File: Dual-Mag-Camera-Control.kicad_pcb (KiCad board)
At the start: 4 copper layers, 152.4 x 96.5 mm, 173 parts, among them J1 ~TRIG_IO, J10 RS-232_2_3, J11 PWR_IN_1, J12 PWR_IN_2, J13 STRB_PWR, J14 CAM_COMPUTE_PWR, J15 5V_5A_PWR, J16 5V_2.5A_PWR, J2 TRIG_IO, J3 ADC_DAC, J4 GPIO, J5 CVS-04TB, J6 CVS-04TB, J7 UART_0_1, J8 UART_2_3, J9 RS-232_0_1, Q1 Si7463DP, Q2 Si7463DP, Q3 Si7463DP, Q4 Si7463DP, Q5 SISS12DN, Q6 Si7463DP, Q7 SISS12DN, Q8 Si7463DP, Q9 Si7463DP, U1 D24V10F5, U10 BME280, U11 S18V20F12, U12 S18V20F12, U13 LTC4412HVIS6, U14 LTC4412HVIS6, U15 LTC4412HVIS6, U16 LTC4412HVIS6, U17 LTC4412HVIS6, U18 DS3231M, U2 INA260, U3 D24V50F5, U4 LowPowerLab-SD-Card, U5 D24V22F5, U6 INA260, U8 MoteinoM0

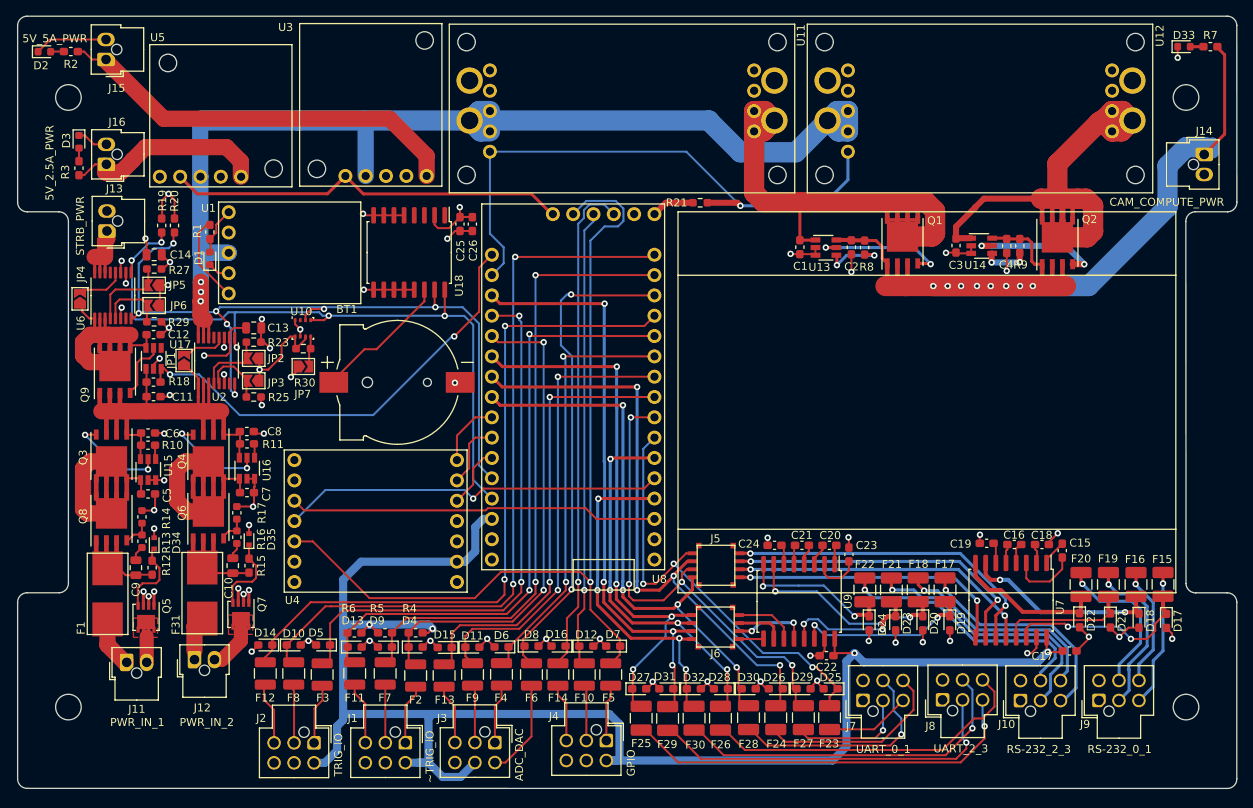
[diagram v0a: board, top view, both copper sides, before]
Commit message: Moved Connectors, NEW PTC Footprint
updated ptc footprints to 0603. Relocated GPIO connectors J1-J4
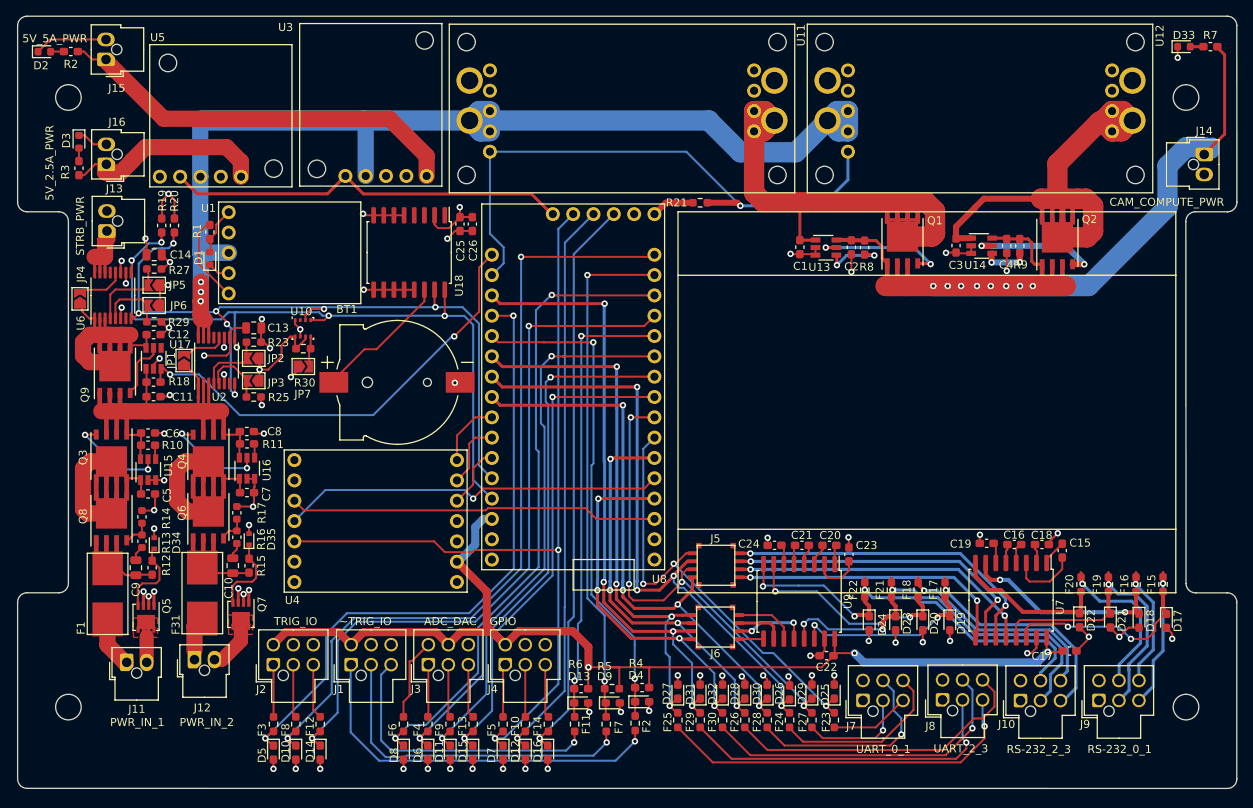
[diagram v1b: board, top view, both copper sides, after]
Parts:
- F10, F11, F12, F13, F14, F2, F3, F4, F5, F6, F7, F8, F9: footprint Resistor_SMD:R_1210_3225Metric -> Resistor_SMD:R_0603_1608Metric_Pad0.98x0.95mm_HandSolder
- F15, F16, F17, F18, F19, F20, F21, F22, F23, F24, F25, F26, F27, F28, F29, F30: footprint Resistor_SMD:R_1210_3225Metric_Pad1.42x2.65mm_HandSolder -> Resistor_SMD:R_0603_1608Metric_Pad0.98x0.95mm_HandSolder
- R5: footprint Resistor_SMD:R_0603_1608Metric_Pad1.05x0.95mm_HandSolder -> Resistor_SMD:R_0603_1608Metric_Pad0.98x0.95mm_HandSolder
- moved D9 29.3 mm to (120.1, 136.0), turned to 0 degrees
- moved R5 29.2 mm to (120.0, 134.3), turned to 0 degrees
- moved R6 29.2 mm to (116.1, 134.3)
- moved D13 29.2 mm to (116.1, 136.0)
- moved D4 29.1 mm to (123.7, 135.9)
- moved R4 29.1 mm to (123.7, 134.1)
- moved F7 28.4 mm to (119.2, 138.7)
- moved F11 28.2 mm to (115.3, 138.7)
- moved F2 28.1 mm to (122.9, 138.6)
- moved D8 20.8 mm to (93.9, 142.2), turned to -90 degrees
- moved D7 19.1 mm to (106.3, 142.2), turned to -90 degrees
- moved F6 17.2 mm to (93.9, 138.7), turned to 90 degrees
- moved D6 16.1 mm to (97.0, 142.2), turned to -90 degrees
- moved J4 15.8 mm to (106.6, 131.2), turned to 90 degrees
- moved D12 15.3 mm to (109.1, 142.2), turned to -90 degrees
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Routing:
- net /3.3V_LDO: track 390.2 -> 333.0 mm, vias 11 -> 10
- net /5V_reg: track 154.1 -> 102.1 mm
- net /TRIG0_1_IO: track 8.44 -> 47.8 mm, vias 0 -> 1
- net /TRIG1_1_IO: track 7.26 -> 42.1 mm, vias 0 -> 1
- net /TRIG4_1_IO: track 7.81 -> 36.5 mm, vias 0 -> 1
- net /COMMS/TX2: track 22.1 -> 50.1 mm, vias 2 -> 3
- net /COMMS/TX2_OUT: track 28.0 -> 0.00 mm, vias 1 -> 0
- net /TRIG4_1: track 78.3 -> 57.3 mm
- net /DAC_OUT: track 61.0 -> 80.7 mm
- net /A3: track 53.6 -> 70.6 mm
- net /GPIO_2: track 57.2 -> 72.2 mm
- net /TRIG1_1: track 78.9 -> 64.6 mm
- net /TRIG0_0: track 69.3 -> 80.1 mm
- net /A4: track 56.5 -> 66.7 mm
- net /GPIO_3: track 62.5 -> 72.2 mm
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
